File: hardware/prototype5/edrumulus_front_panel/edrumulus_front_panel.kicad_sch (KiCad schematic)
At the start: 2 parts, among them J2 Raspberry Pi GPIO pins

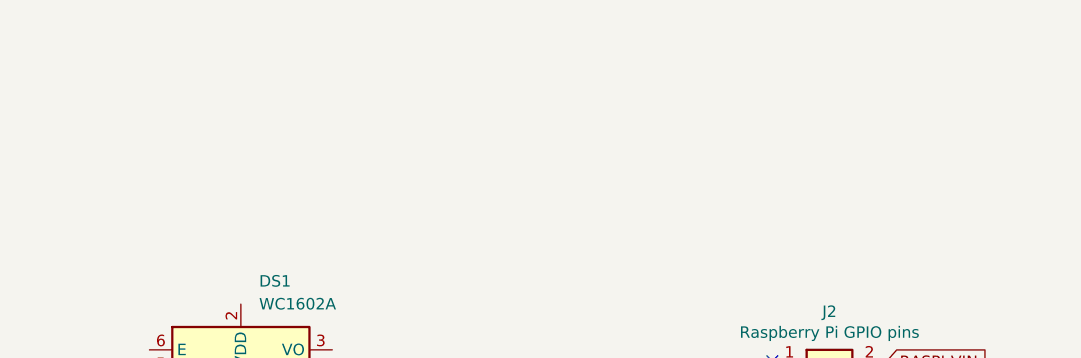
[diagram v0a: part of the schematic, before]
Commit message: adding buttons to the front panel for prototype 5
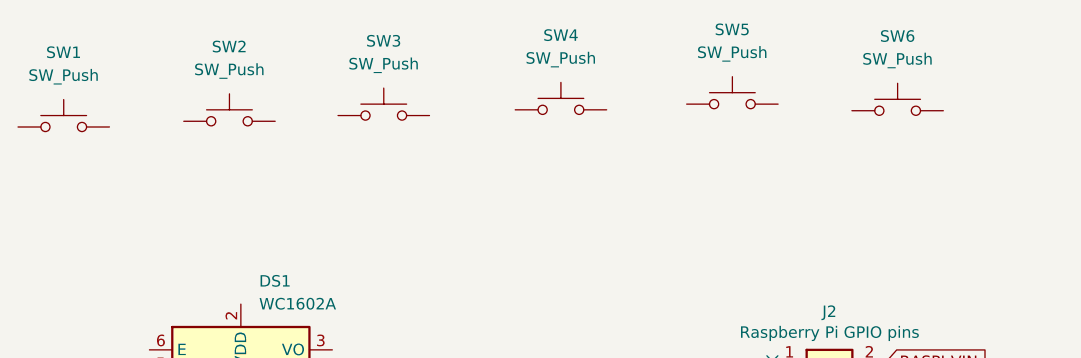
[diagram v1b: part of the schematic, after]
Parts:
- added SW1, SW2, SW3, SW4, SW5, SW6: SW_Push, Button_Switch_THT:SW_PUSH_6mm_H7.3mm, symbol Switch:SW_Push
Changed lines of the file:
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@@
     (pin "MP")
+  )
+  (symbol (lib_id "Switch:SW_Push") (at 163.195 40.64 0) (unit 1)
+    (in_bom yes) (on_board yes) (fields_autoplaced)
+    (property "Reference" "SW4" (id 0) (at 163.195 32.385 0))
+    (property "Value" "SW_Push" (id 1) (at 163.195 34.925 0))
+    (property "Footprint" "Button_Switch_THT:SW_PUSH_6mm_H7.3mm" (id 2) (at 163.195 35.56 0)
+      (effects (font (size 1.27 1.27)) hide)
+    )
+    (property "Datasheet" "~" (id 3) (at 163.195 35.56 0)
+      (effects (font (size 1.27 1.27)) hide)
+    )
+    (pin "1")
+    (pin "2")
+  )
+  (symbol (lib_id "Switch:SW_Push") (at 182.245 40.005 0) (unit 1)
+    (in_bom yes) (on_board yes) (fields_autoplaced)
+    (property "Reference" "SW5" (id 0) (at 182.245 31.75 0))
+    (property "Value" "SW_Push" (id 1) (at 182.245 34.29 0))
+    (property "Footprint" "Button_Switch_THT:SW_PUSH_6mm_H7.3mm" (id 2) (at 182.245 34.925 0)
+      (effects (font (size 1.27 1.27)) hide)
+    )
+    (property "Datasheet" "~" (id 3) (at 182.245 34.925 0)
+      (effects (font (size 1.27 1.27)) hide)
+    )
+    (pin "1")
+    (pin "2")
+  )
+  (symbol (lib_id "Switch:SW_Push") (at 126.365 41.91 0) (unit 1)
+    (in_bom yes) (on_board yes) (fields_autoplaced)
+    (property "Reference" "SW2" (id 0) (at 126.365 33.655 0))
+    (property "Value" "SW_Push" (id 1) (at 126.365 36.195 0))
+    (property "Footprint" "Button_Switch_THT:SW_PUSH_6mm_H7.3mm" (id 2) (at 126.365 36.83 0)
+      (effects (font (size 1.27 1.27)) hide)
+    )
+    (property "Datasheet" "~" (id 3) (at 126.365 36.83 0)
+      (effects (font (size 1.27 1.27)) hide)
+    )
+    (pin "1")
+    (pin "2")
+  )
+  (symbol (lib_id "Switch:SW_Push") (at 107.95 42.545 0) (unit 1)
+    (in_bom yes) (on_board yes) (fields_autoplaced)
+    (property "Reference" "SW1" (id 0) (at 107.95 34.29 0))
+    (property "Value" "SW_Push" (id 1) (at 107.95 36.83 0))
+    (property "Footprint" "Button_Switch_THT:SW_PUSH_6mm_H7.3mm" (id 2) (at 107.95 37.465 0)
+      (effects (font (size 1.27 1.27)) hide)
+    )
+    (property "Datasheet" "~" (id 3) (at 107.95 37.465 0)
+      (effects (font (size 1.27 1.27)) hide)
+    )
+    (pin "1")
+    (pin "2")
+  )
+  (symbol (lib_id "Switch:SW_Push") (at 143.51 41.275 0) (unit 1)
+    (in_bom yes) (on_board yes) (fields_autoplaced)
+    (property "Reference" "SW3" (id 0) (at 143.51 33.02 0))
+    (property "Value" "SW_Push" (id 1) (at 143.51 35.56 0))
+    (property "Footprint" "Button_Switch_THT:SW_PUSH_6mm_H7.3mm" (id 2) (at 143.51 36.195 0)
+      (effects (font (size 1.27 1.27)) hide)
+    )
+    (property "Datasheet" "~" (id 3) (at 143.51 36.195 0)
+      (effects (font (size 1.27 1.27)) hide)
+    )
+    (pin "1")
+    (pin "2")
+  )
+  (symbol (lib_id "Switch:SW_Push") (at 200.6062 40.7405 0) (unit 1)
+    (in_bom yes) (on_board yes) (fields_autoplaced)
+    (property "Reference" "SW6" (id 0) (at 200.6062 32.4855 0))
+    (property "Value" "SW_Push" (id 1) (at 200.6062 35.0255 0))
+    (property "Footprint" "Button_Switch_THT:SW_PUSH_6mm_H7.3mm" (id 2) (at 200.6062 35.6605 0)
+      (effects (font (size 1.27 1.27)) hide)
+    )
+    (property "Datasheet" "~" (id 3) (at 200.6062 35.6605 0)
+      (effects (font (size 1.27 1.27)) hide)
+    )
+    (pin "1")
+    (pin "2")
   )
   (symbol (lib_id "Display_Character:WC1602A") (at 127.635 82.55 0) (unit 1)
@@
       (reference "J2") (unit 1) (value "Raspberry Pi GPIO pins") (footprint "Connector_PinHeader_2.54mm:PinHeader_2x20_P2.54mm_Vertical")
     )
+    (path "/6ce41a48-c5e2-4d5f-8548-1c7b5c309a8a"
+      (reference "SW1") (unit 1) (value "SW_Push") (footprint "Button_Switch_THT:SW_PUSH_6mm_H7.3mm")
+    )
+    (path "/53dd890e-5aba-493f-87ec-8a34bea86d70"
+      (reference "SW2") (unit 1) (value "SW_Push") (footprint "Button_Switch_THT:SW_PUSH_6mm_H7.3mm")
+    )
+    (path "/754700b8-82bc-4d0e-926c-196988658878"
+      (reference "SW3") (unit 1) (value "SW_Push") (footprint "Button_Switch_THT:SW_PUSH_6mm_H7.3mm")
+    )
+    (path "/3423b69d-31f4-49a7-a31b-7a75e0771985"
+      (reference "SW4") (unit 1) (value "SW_Push") (footprint "Button_Switch_THT:SW_PUSH_6mm_H7.3mm")
+    )
+    (path "/47b07f0a-8fd0-430f-a507-f3e6a09cb004"
+      (reference "SW5") (unit 1) (value "SW_Push") (footprint "Button_Switch_THT:SW_PUSH_6mm_H7.3mm")
+    )
+    (path "/ae8e6a57-da88-4fc2-a435-e3e6aa3bc05e"
+      (reference "SW6") (unit 1) (value "SW_Push") (footprint "Button_Switch_THT:SW_PUSH_6mm_H7.3mm")
+    )
   )
